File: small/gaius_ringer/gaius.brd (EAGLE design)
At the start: 33 x 34.3 mm, 30 parts, among them Q1 2N5088, Q2 2N3906-, Q3 2N5088

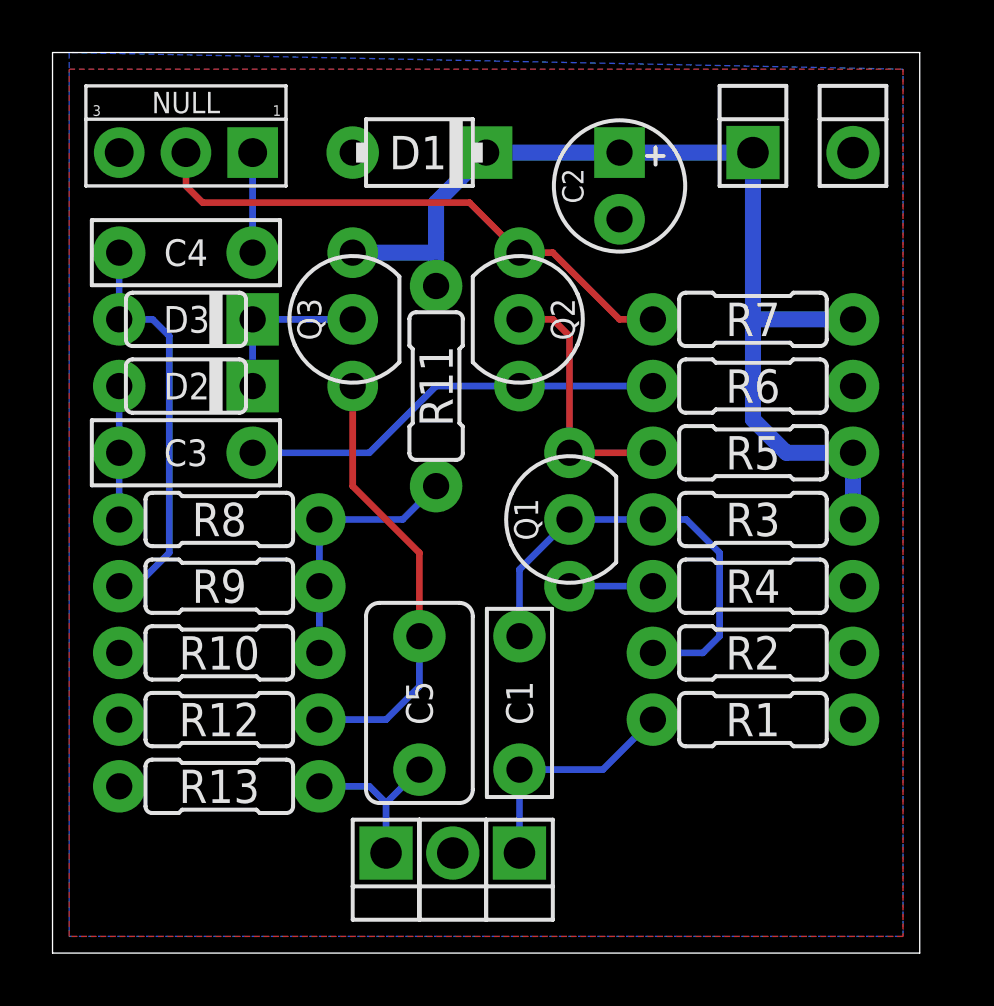
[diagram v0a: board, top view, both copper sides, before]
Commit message: updated Gaius Ringer & Janus Drive, added Chimera Chorus
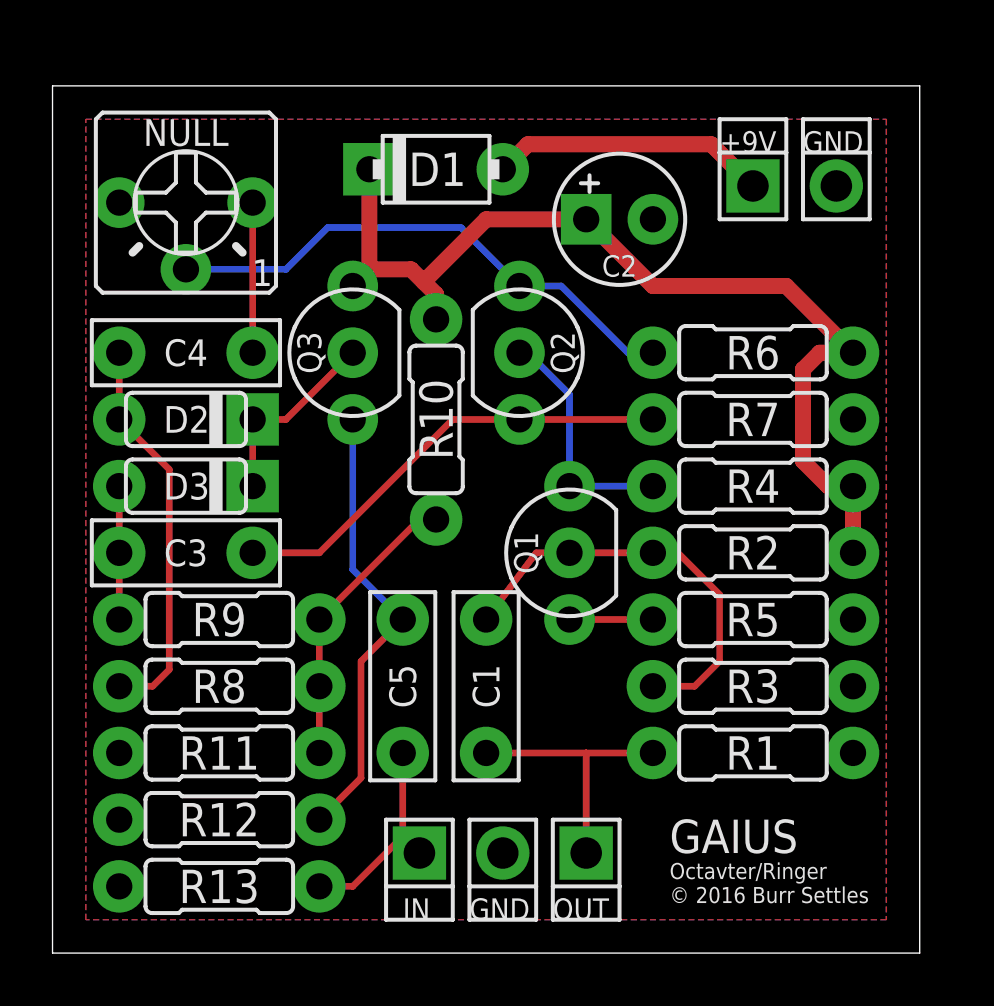
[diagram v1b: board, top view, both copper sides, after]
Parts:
- C5: device capacitors-film:BOX_MED -> capacitors-film:BOX_SMALL
- D1: value 1n4001 -> 1N5817
- NULL: device potentiometers:PADS_SMALL -> potentiometers:2262_TRIM
- Q2: value 2N3906- -> 2N3906
- R2: value 160k -> 470k
- R3: value 560k -> 160k
- R4: value 6k2 -> 18k
- R5: value 18k -> 6k2
- moved R11 16.2 mm to (6.35, 7.62), turned to 0 degrees
- moved R10 12.1 mm to (14.6, 20.3), turned to 90 degrees
- moved R3 6.35 mm to (26.7, 10.2), turned to 180 degrees
- moved R5 6.35 mm to (26.7, 12.7), turned to 180 degrees
- moved R8 6.35 mm to (6.35, 10.2), turned to 180 degrees
- moved D3 6.35 mm to (5.08, 17.8)
- moved C4 3.81 mm to (5.08, 22.9)
- moved C3 3.81 mm to (5.08, 15.2)
- moved R12 3.81 mm to (6.35, 5.08)
- moved R2 3.81 mm to (26.7, 15.2), turned to 0 degrees
- moved R4 3.81 mm to (26.7, 17.8), turned to 0 degrees
- moved R13 3.81 mm to (6.35, 2.54)
- moved R7 3.81 mm to (26.7, 20.3), turned to 180 degrees
- moved PAD2 2.54 mm to (20.3, 3.81)
- moved NULL 1.91 mm to (5.08, 28.6), turned to 180 degrees
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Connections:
- new net N$12: C2.+, D1.C, Q3.1, R10.2, R2.2, R4.2, R6.2
- net +9V: now also D1.A; no longer C2.+, D1.C, Q3.1, R11.2, R3.2, R5.2, R7.2
- net GND: now also R11.1, R3.1, R5.1, R7.1; no longer D1.A, R10.1, R2.1, R4.1, R6.1
- net N$1: now also R4.1; no longer R5.1
- net N$2: now also R5.2; no longer R4.2
- net N$3: now also R2.1, R3.2; no longer R2.2, R3.1
- net N$4: now also D2.A, R8.2; no longer D3.A, R9.2
- net N$5: now also R6.1; no longer R7.1
- net N$6: now also R10.1, R11.2, R8.1, R9.2; no longer R10.2, R11.1, R8.2, R9.1
- net N$8: now also R7.2; no longer R6.2
- net N$9: now also D3.A, R9.1; no longer D2.A, R8.1
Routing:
- net N$12: track 0.00 -> 38.5 mm
- net +9V: track 40.1 -> 10.6 mm
- net N$7: track 3.81 -> 5.71 mm
- net OUT1: track 6.50 -> 8.04 mm
- net N$3: track 17.5 -> 16.3 mm
- net IN1: track 9.04 -> 10.2 mm
- net N$8: track 16.3 -> 17.3 mm
- net N$11: track 6.35 -> 7.40 mm
- net N$6: track 10.1 -> 11.1 mm
- net N$5: track 21.2 -> 20.4 mm
- net N$1: track 9.79 -> 9.23 mm
- net N$10: track 16.8 -> 17.3 mm
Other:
- board size 33 x 34.3 mm -> 33 x 33 mm
- board text added: "+9V"
- board text added: "GAIUS"
- board text added: "GND"
- board text added: "IN"
- board text added: "OUT"
- board text added: "Octavter/Ringer © 2016 Burr Settles"

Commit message: updates to a few small pedals
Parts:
- C2: value 100uF -> 100u
- D2, D3: value 1n34a -> 1N34A
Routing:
- net N$12: track 38.5 -> 39.2 mm
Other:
- board text added: "octavter / ringmod © 2016 burr settles"
- board text removed: "Octavter/Ringer © 2016 Burr Settles"
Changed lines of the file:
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@@
 <wire x1="0" y1="33.02" x2="0" y2="0" width="0" layer="20"/>
 <text x="23.495" y="3.81" size="1.27" layer="25">GAIUS</text>
-<text x="23.495" y="1.905" size="0.6096" layer="25">Octavter/Ringer
-© 2016 Burr Settles</text>
+<text x="23.495" y="1.905" size="0.6096" layer="25">octavter / ringmod
+© 2016 burr settles</text>
 <text x="13.335" y="1.27" size="0.8128" layer="25">IN</text>
 <text x="15.875" y="1.27" size="0.8128" layer="25">GND</text>
@@
 <element name="C3" library="capacitors-film" package="BOX_SMALL" value="47n" x="5.08" y="15.24"/>
 <element name="C4" library="capacitors-film" package="BOX_SMALL" value="47n" x="5.08" y="22.86" rot="R180"/>
-<element name="C2" library="capacitors-elec" package="050_020_1" value="100uF" x="21.59" y="27.94"/>
-<element name="D2" library="diodes" package="DO35-2" value="1n34a" x="5.08" y="20.32" rot="R180"/>
-<element name="D3" library="diodes" package="DO35-2" value="1n34a" x="5.08" y="17.78" rot="R180"/>
+<element name="C2" library="capacitors-elec" package="050_020_1" value="100u" x="21.59" y="27.94"/>
+<element name="D2" library="diodes" package="DO35-2" value="1N34A" x="5.08" y="20.32" rot="R180"/>
+<element name="D3" library="diodes" package="DO35-2" value="1N34A" x="5.08" y="17.78" rot="R180"/>
 <element name="D1" library="diodes" package="DO41-2" value="1N5817" x="14.605" y="29.845"/>
 <element name="NULL" library="potentiometers" package="2262_TRIM" value="25kB" x="5.08" y="28.575" rot="R180"/>
@@
 <contactref element="PAD4" pad="1"/>
 <contactref element="PAD4" pad="1"/>
-<contactref element="PAD3" pad="1"/>
-<contactref element="PAD3" pad="1"/>
-<contactref element="C2" pad="-"/>
 <polygon width="0.254" layer="16">
 <vertex x="1.27" y="31.75"/>
@@
 <vertex x="1.27" y="1.27"/>
 </polygon>
+<contactref element="C2" pad="-"/>
+<contactref element="PAD3" pad="1"/>
+<contactref element="PAD3" pad="1"/>
 </signal>
 <signal name="N$5">
@@
 <contactref element="R10" pad="2"/>
 <contactref element="D1" pad="C"/>
-<wire x1="12.065" y1="29.845" x2="12.065" y2="26.035" width="0.6096" layer="1"/>
-<wire x1="12.065" y1="26.035" x2="11.43" y2="25.4" width="0.6096" layer="1"/>
-<wire x1="14.605" y1="24.13" x2="14.605" y2="25.0825" width="0.6096" layer="1"/>
-<wire x1="14.605" y1="25.0825" x2="14.12875" y2="25.55875" width="0.6096" layer="1"/>
-<wire x1="14.12875" y1="25.55875" x2="13.6525" y2="26.035" width="0.6096" layer="1"/>
-<wire x1="13.6525" y1="26.035" x2="12.065" y2="26.035" width="0.6096" layer="1"/>
-<wire x1="20.32" y1="27.94" x2="16.51" y2="27.94" width="0.6096" layer="1"/>
-<wire x1="16.51" y1="27.94" x2="14.12875" y2="25.55875" width="0.6096" layer="1"/>
 <wire x1="20.32" y1="27.94" x2="22.86" y2="25.4" width="0.6096" layer="1"/>
 <wire x1="22.86" y1="25.4" x2="27.94" y2="25.4" width="0.6096" layer="1"/>
-<wire x1="27.94" y1="25.4" x2="30.48" y2="22.86" width="0.6096" layer="1"/>
-<wire x1="30.48" y1="22.86" x2="29.21" y2="22.86" width="0.6096" layer="1"/>
-<wire x1="29.21" y1="22.86" x2="28.575" y2="22.225" width="0.6096" layer="1"/>
-<wire x1="28.575" y1="22.225" x2="28.575" y2="18.7325" width="0.6096" layer="1"/>
-<wire x1="28.575" y1="18.7325" x2="29.5275" y2="17.78" width="0.6096" layer="1"/>
-<wire x1="29.5275" y1="17.78" x2="30.48" y2="17.78" width="0.6096" layer="1"/>
 <wire x1="30.48" y1="17.78" x2="30.48" y2="15.24" width="0.6096" layer="1"/>
+<wire x1="12.065" y1="29.845" x2="12.065" y2="27.94" width="0.6096" layer="1"/>
+<wire x1="12.065" y1="27.94" x2="12.065" y2="26.67" width="0.6096" layer="1"/>
+<wire x1="11.43" y1="26.035" x2="12.065" y2="26.67" width="0.6096" layer="1"/>
+<wire x1="11.43" y1="25.4" x2="11.43" y2="26.035" width="0.6096" layer="1"/>
+<wire x1="20.32" y1="27.94" x2="14.605" y2="27.94" width="0.6096" layer="1"/>
+<wire x1="14.605" y1="27.94" x2="12.065" y2="27.94" width="0.6096" layer="1"/>
+<wire x1="14.605" y1="24.13" x2="14.605" y2="27.94" width="0.6096" layer="1"/>
+<wire x1="27.94" y1="25.4" x2="27.94" y2="22.86" width="0.6096" layer="1"/>
+<wire x1="27.94" y1="22.86" x2="27.94" y2="20.32" width="0.6096" layer="1"/>
+<wire x1="27.94" y1="20.32" x2="30.48" y2="17.78" width="0.6096" layer="1"/>
+<wire x1="30.48" y1="22.86" x2="27.94" y2="22.86" width="0.6096" layer="1"/>
 </signal>
 </signals>

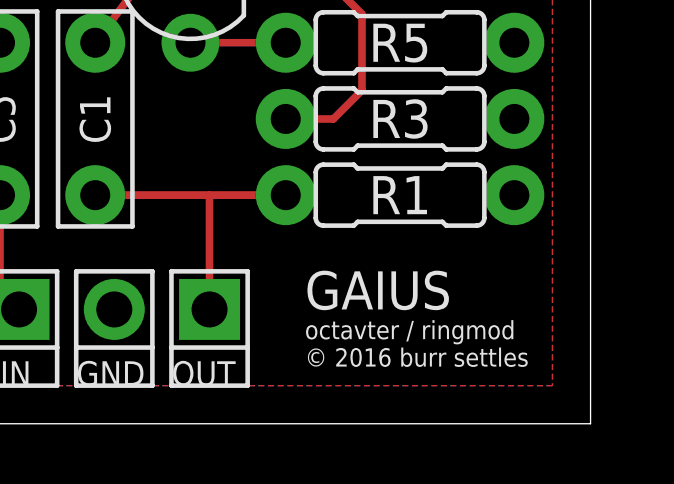
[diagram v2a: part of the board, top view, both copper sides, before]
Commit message: added phaser schematic; minor board tweaks
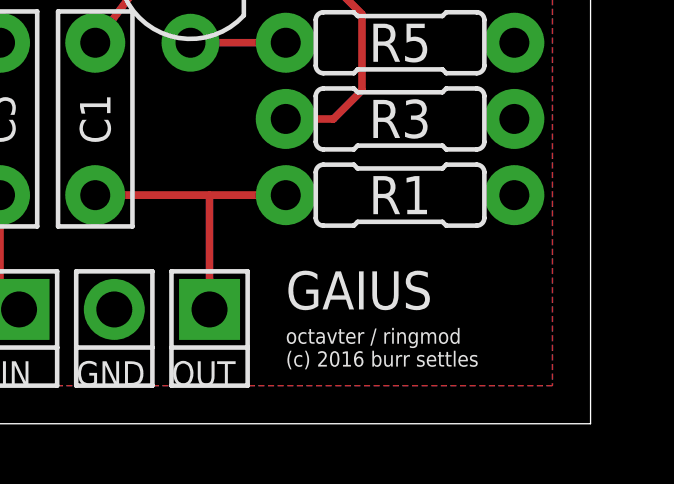
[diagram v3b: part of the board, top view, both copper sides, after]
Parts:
- D2, D3: value 1N34A -> 1N914
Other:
- board text added: "octavter / ringmod (c) 2016 burr settles"
- board text removed: "octavter / ringmod © 2016 burr settles"
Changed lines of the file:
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@@
 <wire x1="33.02" y1="33.02" x2="0" y2="33.02" width="0" layer="20"/>
 <wire x1="0" y1="33.02" x2="0" y2="0" width="0" layer="20"/>
-<text x="23.495" y="3.81" size="1.27" layer="25">GAIUS</text>
-<text x="23.495" y="1.905" size="0.6096" layer="25">octavter / ringmod
-© 2016 burr settles</text>
+<text x="22.86" y="3.81" size="1.27" layer="25" font="vector">GAIUS</text>
+<text x="22.86" y="1.905" size="0.508" layer="25" font="vector">octavter / ringmod
+(c) 2016 burr settles</text>
 <text x="13.335" y="1.27" size="0.8128" layer="25">IN</text>
 <text x="15.875" y="1.27" size="0.8128" layer="25">GND</text>
@@
 <element name="C4" library="capacitors-film" package="BOX_SMALL" value="47n" x="5.08" y="22.86" rot="R180"/>
 <element name="C2" library="capacitors-elec" package="050_020_1" value="100u" x="21.59" y="27.94"/>
-<element name="D2" library="diodes" package="DO35-2" value="1N34A" x="5.08" y="20.32" rot="R180"/>
-<element name="D3" library="diodes" package="DO35-2" value="1N34A" x="5.08" y="17.78" rot="R180"/>
+<element name="D2" library="diodes" package="DO35-2" value="1N914" x="5.08" y="20.32" rot="R180"/>
+<element name="D3" library="diodes" package="DO35-2" value="1N914" x="5.08" y="17.78" rot="R180"/>
 <element name="D1" library="diodes" package="DO41-2" value="1N5817" x="14.605" y="29.845"/>
 <element name="NULL" library="potentiometers" package="2262_TRIM" value="25kB" x="5.08" y="28.575" rot="R180"/>
